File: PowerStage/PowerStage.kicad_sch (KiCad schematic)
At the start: 27 parts, among them J1 Conn_01x02, J2 Conn_01x02, J3 Conn_01x03, Q1 IRFZ44N, Q2 IRFZ44N, SW2 SW_SPDT_XKB_DMx-xxxx-1, U1 IR2110

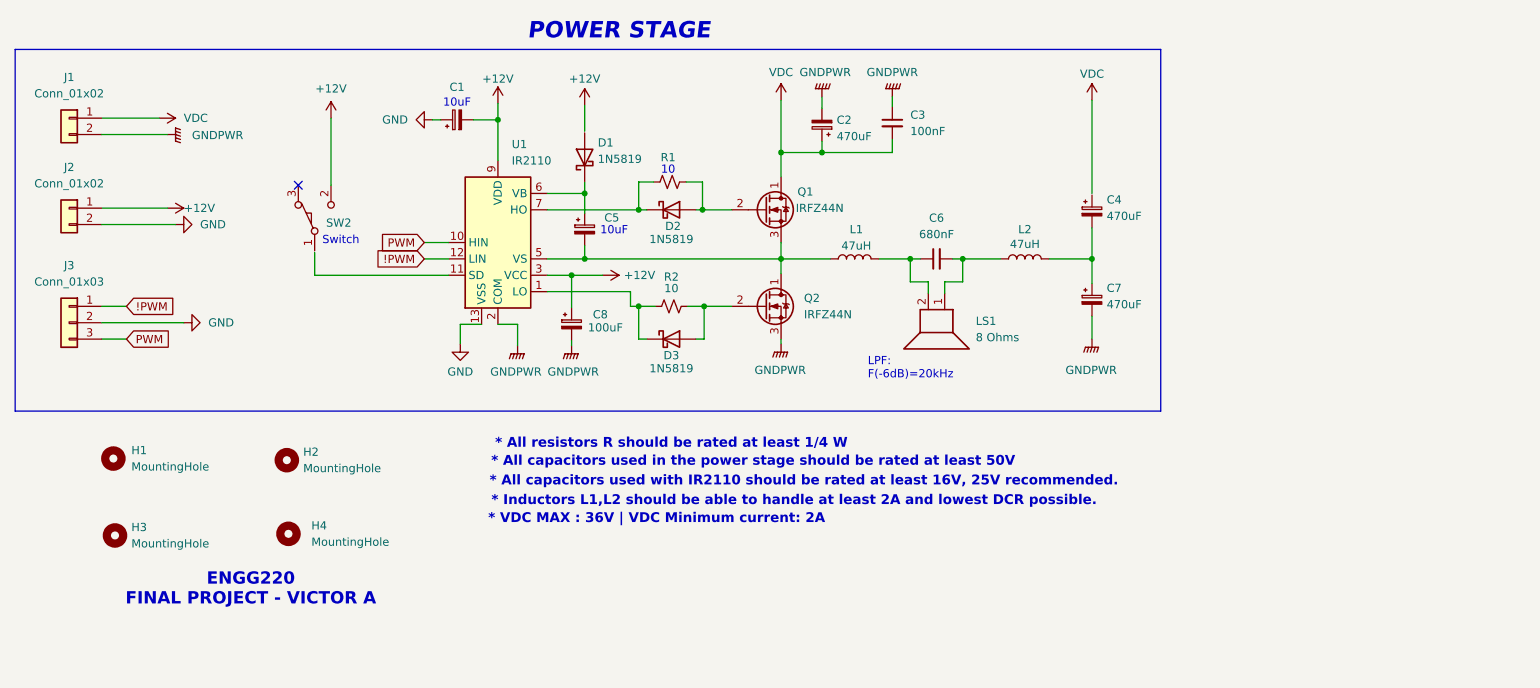
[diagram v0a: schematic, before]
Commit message: Init Full Bridge Topology
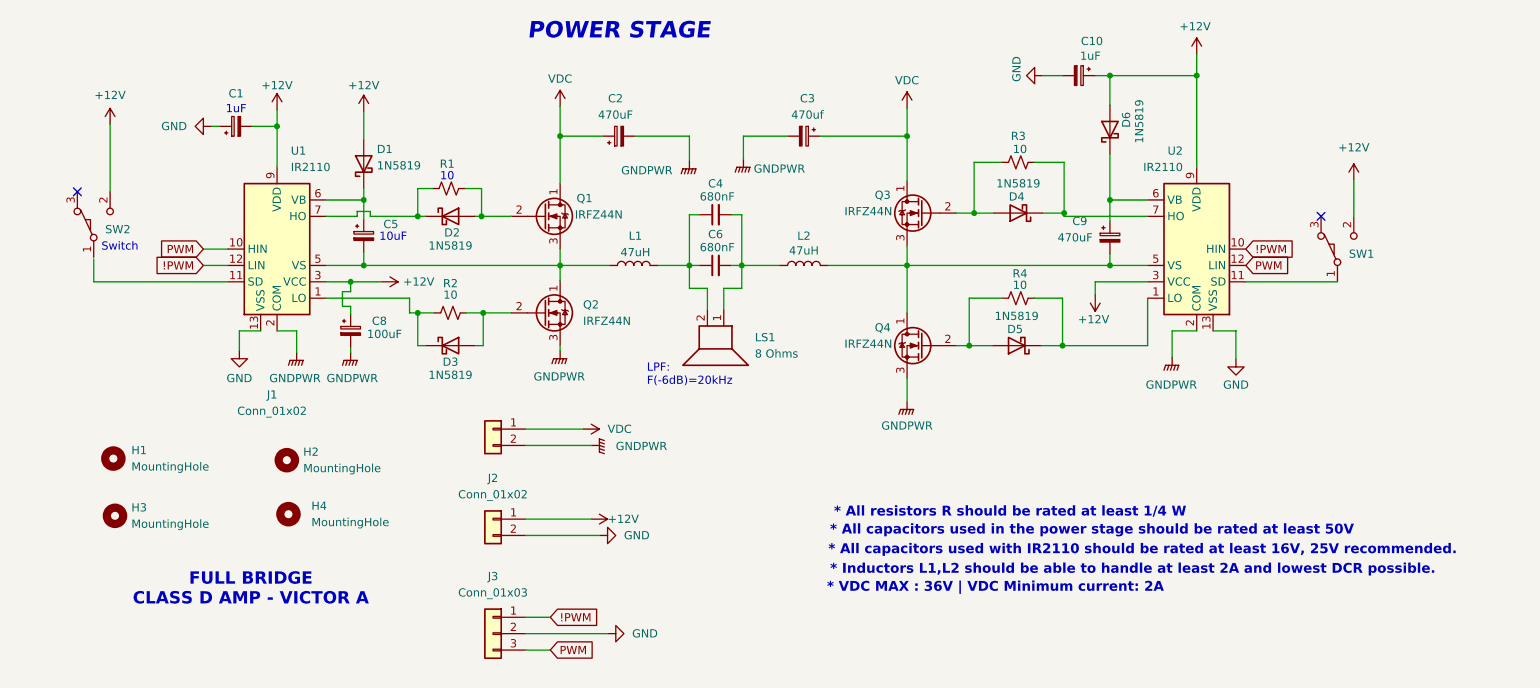
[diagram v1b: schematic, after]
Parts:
- removed C3: 100nF, symbol Device:C_Small
- removed C4, C7: 470uF, symbol Device:C_Polarized_Small
- added C10: 1uF, symbol Device:C_Polarized_Small
- added C3: 470uf, symbol Device:C_Polarized_Small
- added C4: 680nF, symbol Device:C_Small
- added C9: 470uF, symbol Device:C_Polarized_Small
- added D4, D5, D6: 1N5819, Diode_THT:D_DO-41_SOD81_P10.16mm_Horizontal, symbol Diode:1N5819
- added Q3, Q4: IRFZ44N, Package_DirectFET:DirectFET_MF, symbol Transistor_FET:IRF40DM229
- added R3, R4: 10, symbol Device:R_Small_US
- added SW1: SW_SPDT_XKB_DMx-xxxx-1, symbol Switch:SW_SPDT_XKB_DMx-xxxx-1
- added U2: IR2110, Package_DIP:DIP-14_W7.62mm, symbol Driver_FET:IR2110
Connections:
- net !PWM: now also U2.10 (HIN)
- net +12V: now also D1.2 (A), C10.1, D6.2 (A), SW1.2 (B), U2.3 (VCC), U2.9 (VDD)
- net GND: now also C10.2, U2.13 (VSS)
- net GNDPWR: now also C3.2, Q4.3 (S), U2.2 (COM)
- net PWM: now also U2.12 (LIN)
- net VDC: now also C3.1, Q3.1 (D)
- net at L2.2: now also C9.2, Q3.3 (S), Q4.1 (D), U2.5 (VS)
- net at C6.2, L2.1, LS1.1: now also C4.2
- net at C6.1, L1.2, LS1.2: now also C4.1
- net at C5.2, Q1.3 (S), Q2.1 (D)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: now also L1.1
- new net: D4.2 (A), Q3.2 (G), R3.1
- new net: C9.1, D6.1 (K), U2.6 (VB)
- new net: SW1.1 (A), U2.11 (SD)
- new net: D4.1 (K), R3.2, U2.7 (HO)
- new net: D5.2 (A), Q4.2 (G), R4.1
- new net: D5.1 (K), R4.2, U2.1 (LO)
- no-connect marks 1 -> 2
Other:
- note added: "1uF"
- note added: "FULL BRIDGE CLASS D AMP - VICTOR A"
- note removed: "ENGG220 FINAL PROJECT - VICTOR A"
- moved on the sheet: C1, C5, C6, C8, D1, D2, D3, H3, H4, J1, J2, J3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

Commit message: Init pcb layout
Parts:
- removed SW1, SW2: SW_SPDT_XKB_DMx-xxxx-1, symbol Switch:SW_SPDT_XKB_DMx-xxxx-1
- added C11, C7: 100nF, Capacitor_THT:CP_Radial_D12.5mm_P5.00mm, symbol Device:C_Polarized_Small
- added JP1, JP2: SolderJumper_2_Open, Jumper:SolderJumper-2_P1.3mm_Open_Pad1.0x1.5mm, symbol Jumper:SolderJumper_2_Open
- added R5, R6: 10k, Resistor_THT:R_Axial_DIN0207_L6.3mm_D2.5mm_P7.62mm_Horizontal, symbol Device:R_Small_US
- C1, C10, C5: footprint (none) -> Capacitor_THT:CP_Radial_D5.0mm_P2.00mm
- C2, C3: footprint (none) -> Capacitor_THT:CP_Radial_D12.5mm_P5.00mm
- C4, C6: footprint (none) -> Capacitor_THT:C_Rect_L24.0mm_W8.3mm_P22.50mm_MKT
- C8: footprint (none) -> Capacitor_THT:CP_Radial_D8.0mm_P3.80mm
- C9: value 470uF -> 10uF; footprint (none) -> Capacitor_THT:CP_Radial_D5.0mm_P2.00mm
- H1, H2, H3, H4: footprint (none) -> MountingHole:MountingHole_3.2mm_M3_Pad_Via
- J1, J2: footprint (none) -> Connector_JST:JST_XH_B2B-XH-A_1x02_P2.50mm_Vertical
- J3: footprint (none) -> Connector_JST:JST_XH_B3B-XH-A_1x03_P2.50mm_Vertical
- L1, L2: footprint (none) -> Inductor_SMD:L_12x12mm_H6mm
- LS1: footprint (none) -> Connector_JST:JST_VH_B2P-VH_1x02_P3.96mm_Vertical
- Q1, Q2, Q3, Q4: footprint Package_DirectFET:DirectFET_MF -> Package_TO_SOT_THT:TO-220-3_Vertical
- R1, R2, R3, R4: footprint (none) -> Resistor_THT:R_Axial_DIN0207_L6.3mm_D2.5mm_P7.62mm_Horizontal
- U1, U2: footprint Package_DIP:DIP-14_W7.62mm -> Package_DIP:DIP-14_W7.62mm_Socket
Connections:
- net +12V: now also JP1.2 (B), JP2.2 (B)
- net GND: now also R5.2, R6.2
- net GNDPWR: now also C11.2, C7.2
- net VDC: now also C11.1, C7.1
- net at U2.11 (SD): now also JP1.1 (A), R5.1
- net at U1.11 (SD): now also JP2.1 (A), R6.1
- no-connect marks 2 -> 0
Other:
- note removed: "Switch"
- moved on the sheet: J1, J2, J3

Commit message: PCB desing init
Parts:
- added TP1, TP2, TP3, TP4, TP5, TP6, TP7, TP8, TP9: TestPoint, TestPoint:TestPoint_Keystone_5010-5014_Multipurpose, symbol Connector:TestPoint
- C11, C7: footprint Capacitor_THT:CP_Radial_D12.5mm_P5.00mm -> Capacitor_THT:C_Disc_D3.8mm_W2.6mm_P2.50mm
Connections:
- net +12V: now also R5.2, R6.2; no longer JP1.2 (B), JP2.2 (B)
- net GND: now also JP1.2 (B), JP2.2 (B), TP9.1; no longer R5.2, R6.2
- net GNDPWR: now also TP4.1, TP8.1
- net at D4.2 (A), Q3.2 (G), R3.1: now also TP5.1
- net at C9.2, L2.2, Q3.3 (S)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: now also TP6.1
- net at C5.2, L1.1, Q1.3 (S)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: now also TP2.1
- net at D3.2 (A), Q2.2 (G), R2.2: now also TP3.1
- net at D2.2 (A), Q1.2 (G), R1.2: now also TP1.1
- net at D5.2 (A), Q4.2 (G), R4.1: now also TP7.1

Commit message: Rev 1.0 Gerber
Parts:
- J1: footprint Connector_JST:JST_XH_B2B-XH-A_1x02_P2.50mm_Vertical -> Connector_JST:JST_VH_B2P-VH_1x02_P3.96mm_Vertical
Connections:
- net at C4.1, C6.1, LS1.2: now also L1.1; no longer L1.2
- net at C5.2, Q1.3 (S), Q2.1 (D)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: now also L1.2; no longer L1.1
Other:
- moved on the sheet: L1
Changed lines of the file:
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@@
 		(on_board yes)
 		(dnp no)
-		(fields_autoplaced yes)
 		(property "Reference" "R6"
 			(at 41.91 59.1819 0)
@@
 					(size 1.27 1.27)
 				)
-				(justify left)
+				(justify right)
 			)
 		)
@@
 			)
 		)
-		(property "Footprint" "Connector_JST:JST_XH_B2B-XH-A_1x02_P2.50mm_Vertical"
+		(property "Footprint" "Connector_JST:JST_VH_B2P-VH_1x02_P3.96mm_Vertical"
 			(at 92.202 80.264 0)
 			(effects
@@
 	(symbol
 		(lib_id "Device:L")
-		(at 112.268 52.324 90)
+		(at 112.268 52.324 270)
+		(mirror x)
 		(unit 1)
 		(exclude_from_sim no)
@@
 		(dnp no)
 		(property "Reference" "L1"
-			(at 112.522 47.752 90)
+			(at 112.014 47.752 90)
 			(effects
 				(font
@@
 		)
 		(property "Value" "47uH"
-			(at 112.522 50.292 90)
+			(at 112.014 50.292 90)
 			(effects
 				(font

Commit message: Revision 1.1 in progress
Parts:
- removed C4: 680nF, Capacitor_THT:C_Rect_L24.0mm_W8.3mm_P22.50mm_MKT, symbol Device:C_Small
- removed JP1, JP2: SolderJumper_2_Open, Jumper:SolderJumper-2_P1.3mm_Open_Pad1.0x1.5mm, symbol Jumper:SolderJumper_2_Open
- removed Q1, Q2, Q3, Q4: IRFZ44N, Package_TO_SOT_THT:TO-220-3_Vertical, symbol Transistor_FET:IRF40DM229
- removed R5, R6: 10k, Resistor_THT:R_Axial_DIN0207_L6.3mm_D2.5mm_P7.62mm_Horizontal, symbol Device:R_Small_US
- added C12: 100nF 1206, Capacitor_SMD:C_1206_3216Metric, symbol Device:C_Small
- added C13: 100nF-1206, Capacitor_SMD:C_1206_3216Metric, symbol Device:C_Small
- added Q1, Q2, Q3, Q4: IRFB4227PBF, lcsc_footprints:C2652_TO-220-3_L10_0-W4_5-P2_54-L, symbol lcsc_imported:IRFB4227PBF
- added R5, R6: 10k-1206, Resistor_SMD:R_1206_3216Metric, symbol Device:R_Small
- added SW1, SW2: K2-2235D-F1, lcsc_footprints:C108742_SW-TH_K2-2235D-F1, symbol lcsc_imported:K2-2235D-F1
- R1, R2, R3, R4: footprint Resistor_THT:R_Axial_DIN0207_L6.3mm_D2.5mm_P7.62mm_Horizontal -> Resistor_SMD:R_1206_3216Metric
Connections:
- net +12V: now also C1.1, SW1.1, SW2.1; no longer C1.2
- net GND: now also C1.2, C11.2, C2.2, C3.2, C7.2, C8.2, J1.2 (Pin_2), TP8.1, U1.2 (COM), U2.2 (COM), C12.2, C13.2, Q2.3 (S), Q4.3 (S), R5.2, R6.2, SW1.3, SW2.3; no longer C1.1
- net VDC: now also Q1.2 (D), Q3.2 (D)
- net at C9.2, L2.2, TP6.1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: now also Q3.3 (S), Q4.2 (D)
- net at D4.2 (A), R3.1, TP5.1: now also Q3.1 (G)
- net at D2.2 (A), R1.2, TP1.1: now also Q1.1 (G)
- net at C5.2, L1.2, TP2.1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: now also Q1.3 (S), Q2.2 (D)
- net at D3.2 (A), R2.2, TP3.1: now also Q2.1 (G)
- net at D5.2 (A), R4.1, TP7.1: now also Q4.1 (G)
- net at U1.11 (SD): now also C12.1, R5.1, SW1.2
- net at U2.11 (SD): now also C13.1, R6.1, SW2.2
- removed net GNDPWR: C11.2, C2.2, C3.2, C7.2, C8.2, J1.2 (Pin_2), TP4.1, TP8.1, U1.2 (COM), U2.2 (COM)
- no-connect marks 0 -> 6
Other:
- moved on the sheet: C1, C10, C11, C6, C7

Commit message: Rev 1.1 progress
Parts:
- removed L1, L2: 47uH, Inductor_SMD:L_12x12mm_H6mm, symbol Device:L
- added C4: 100uF, Capacitor_THT:CP_Radial_D8.0mm_P3.80mm, symbol Device:C_Polarized_Small
- added L1, L2: MDA1365-470M, lcsc_footprints:C2847587_IND-SMD_L13_5-W12_6_TMPA1265SP-100MN-D, symbol lcsc_imported:MDA1365-470M
- C11, C7: footprint Capacitor_THT:C_Disc_D3.8mm_W2.6mm_P2.50mm -> Capacitor_SMD:C_1206_3216Metric
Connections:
- net +12V: now also C4.1
- net GND: now also C4.2
- net at D2.2 (A), R1.2, TP1.1: no longer Q1.1 (G)
- net at C5.2, Q1.3 (S), Q2.2 (D)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: now also L1.1
- net at C6.2, LS1.1: now also L2.1
- net at C6.1, LS1.2: now also L1.2
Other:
- note added: "* VDC MAX : 36V | VDC Maximum current: 2A"
- note removed: "* VDC MAX : 36V | VDC Minimum current: 2A"

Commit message: PCB layout progress
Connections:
- net at C9.2, Q3.3 (S), Q4.2 (D)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: now also L2.2
- net at L2.1, LS1.1: now also C6.1; no longer C6.2
- net at L1.2, LS1.2: now also C6.2; no longer C6.1
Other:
- moved on the sheet: C6
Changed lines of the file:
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@@
 	)
 	(junction
-		(at 154.686 52.324)
+		(at 154.94 52.07)
 		(diameter 0)
 		(color 0 0 0 0)
@@
 	(wire
 		(pts
-			(xy 154.686 52.324) (xy 154.686 59.69)
+			(xy 154.94 52.07) (xy 154.686 59.69)
 		)
 		(stroke
@@
 	(wire
 		(pts
-			(xy 154.686 52.324) (xy 162.56 52.324)
+			(xy 154.94 52.07) (xy 162.56 52.324)
 		)
 		(stroke
@@
 	(wire
 		(pts
-			(xy 154.686 49.276) (xy 154.686 52.324)
+			(xy 154.686 49.276) (xy 154.94 52.07)
 		)
 		(stroke
@@
 	(symbol
 		(lib_id "Device:C_Small")
-		(at 124.968 47.244 90)
+		(at 124.968 47.244 270)
+		(mirror x)
 		(unit 1)
 		(exclude_from_sim no)
@@
 		)
 		(property "Value" "680nF"
-			(at 125.222 44.45 90)
+			(at 124.714 44.45 90)
 			(effects
 				(font
@@
 		(on_board yes)
 		(dnp no)
-		(fields_autoplaced yes)
 		(property "Reference" "L2"
 			(at 142.24 45.72 0)

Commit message: PCB layout progress
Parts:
- removed C2: 470uF, Capacitor_THT:CP_Radial_D12.5mm_P5.00mm, symbol Device:C_Polarized_Small
- removed C3: 470uf, Capacitor_THT:CP_Radial_D12.5mm_P5.00mm, symbol Device:C_Polarized_Small
- added C2, C3: 470uF 16V, lcsc_footprints:C3341_CAP-SMD_BD8_0-L8_3-W8_3-FD, symbol lcsc_imported:470uF_16V
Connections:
- net GND: now also C2.2, C3.2
- net VDC: now also C2.1, C3.1
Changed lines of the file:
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@@
 	)
 	(junction
-		(at 165.1 44.196)
+		(at 154.686 32.258)
 		(diameter 0)
 		(color 0 0 0 0)
 	)
 	(junction
-		(at 88.646 44.704)
+		(at 165.1 44.196)
 		(diameter 0)
 		(color 0 0 0 0)
 	)
 	(junction
-		(at 100.838 32.258)
+		(at 88.646 44.704)
 		(diameter 0)
 		(color 0 0 0 0)
@@
 	)
 	(junction
-		(at 211.582 54.864)
+		(at 100.838 30.226)
 		(diameter 0)
 		(color 0 0 0 0)
 	)
 	(junction
-		(at 87.376 59.69)
+		(at 211.582 54.864)
 		(diameter 0)
 		(color 0 0 0 0)
 	)
 	(junction
-		(at 154.686 32.258)
+		(at 87.376 59.69)
 		(diameter 0)
 		(color 0 0 0 0)
@@
 	(wire
 		(pts
+			(xy 129.286 32.258) (xy 134.874 32.258)
+		)
+		(stroke
+			(width 0)
+			(type default)
+		)
+	)
+	(wire
+		(pts
 			(xy 186.182 50.546) (xy 186.182 52.324)
 		)
@@
 	(wire
 		(pts
+			(xy 154.686 32.258) (xy 154.686 34.29)
+		)
+		(stroke
+			(width 0)
+			(type default)
+		)
+	)
+	(wire
+		(pts
 			(xy 216.916 54.864) (xy 216.916 57.15)
 		)
@@
 	(wire
 		(pts
-			(xy 100.838 32.258) (xy 100.838 33.528)
-		)
-		(stroke
-			(width 0)
-			(type default)
-		)
-	)
-	(wire
-		(pts
 			(xy 165.1 44.196) (xy 165.1 36.322)
 		)
@@
 	(wire
 		(pts
-			(xy 154.686 34.29) (xy 154.686 32.258)
+			(xy 154.686 27.94) (xy 154.686 32.258)
 		)
 		(stroke
@@
 	(wire
 		(pts
-			(xy 154.686 27.94) (xy 154.686 32.258)
-		)
-		(stroke
-			(width 0)
-			(type default)
-		)
-	)
-	(wire
-		(pts
 			(xy 162.306 44.196) (xy 165.1 44.196)
 		)
@@
 	(wire
 		(pts
+			(xy 113.538 30.226) (xy 120.904 30.226)
+		)
+		(stroke
+			(width 0)
+			(type default)
+		)
+	)
+	(wire
+		(pts
 			(xy 97.282 109.474) (xy 101.092 109.474)
 		)
@@
 	(wire
 		(pts
+			(xy 100.838 30.226) (xy 100.838 33.528)
+		)
+		(stroke
+			(width 0)
+			(type default)
+		)
+	)
+	(wire
+		(pts
 			(xy 178.816 57.404) (xy 178.816 64.77)
 		)
@@
 	(wire
 		(pts
+			(xy 100.838 30.226) (xy 105.918 30.226)
+		)
+		(stroke
+			(width 0)
+			(type default)
+		)
+	)
+	(wire
+		(pts
 			(xy 207.264 54.864) (xy 211.582 54.864)
 		)
@@
 	(wire
 		(pts
-			(xy 100.838 27.686) (xy 100.838 32.258)
+			(xy 100.838 27.686) (xy 100.838 30.226)
 		)
 		(stroke
@@
 	(wire
 		(pts
-			(xy 112.522 32.258) (xy 120.904 32.258)
-		)
-		(stroke
-			(width 0)
-			(type default)
-		)
-	)
-	(wire
-		(pts
 			(xy 166.37 56.388) (xy 162.306 56.388)
 		)
@@
 	(wire
 		(pts
-			(xy 120.904 32.258) (xy 120.904 36.068)
+			(xy 120.904 30.226) (xy 120.904 36.068)
 		)
 		(stroke
@@
 	(wire
 		(pts
-			(xy 69.342 44.704) (xy 69.342 43.942)
+			(xy 142.494 32.258) (xy 154.686 32.258)
 		)
 		(stroke
@@
 	(wire
 		(pts
-			(xy 141.224 32.258) (xy 154.686 32.258)
-		)
-		(stroke
-			(width 0)
-			(type default)
-		)
-	)
-	(wire
-		(pts
-			(xy 100.838 32.258) (xy 107.442 32.258)
+			(xy 69.342 44.704) (xy 69.342 43.942)
 		)
 		(stroke
@@
 	(wire
 		(pts
-			(xy 129.286 32.258) (xy 136.144 32.258)
-		)
-		(stroke
-			(width 0)
-			(type default)
-		)
-	)
-	(wire
-		(pts
 			(xy 44.196 61.976) (xy 44.196 63.5)
 		)
@@
 	)
 	(symbol
-		(lib_id "Device:C_Polarized_Small")
-		(at 109.982 32.258 90)
+		(lib_id "lcsc_imported:470uF_16V")
+		(at 109.728 30.226 0)
 		(unit 1)
 		(exclude_from_sim no)
@@
 		(fields_autoplaced yes)
 		(property "Reference" "C2"
-			(at 109.4359 26.416 90)
+			(at 109.1209 23.368 0)
 			(effects
 				(font
@@
 			)
 		)
-		(property "Value" "470uF"
-			(at 109.4359 28.956 90)
+		(property "Value" "470uF 16V"
+			(at 109.1209 25.908 0)
 			(effects
 				(font
@@
 			)
 		)
-		(property "Footprint" "Capacitor_THT:CP_Radial_D12.5mm_P5.00mm"
-			(at 109.982 32.258 0)
+		(property "Footprint" "lcsc_footprints:C3341_CAP-SMD_BD8_0-L8_3-W8_3-FD"
+			(at 109.728 40.386 0)
 			(effects
 				(font
@@
 			)
 		)
-		(property "Datasheet" "~"
-			(at 109.982 32.258 0)
+		(property "Datasheet" "https://wmsc.lcsc.com/wmsc/upload/file/pdf/v2/lcsc/2304140030_Honor-Elec-RVT1C471M0810_C3341.pdf"
+			(at 107.442 30.099 0)
 			(effects
 				(font
@@
 			)
 		)
-		(property "Description" "Polarized capacitor, small symbol"
-			(at 109.982 32.258 0)
+		(property "Description" "470uF 16V"
+			(at 109.728 30.226 0)
+			(effects
+				(font
+					(size 1.27 1.27)
+				)
+				(hide yes)
+			)
+		)
+		(property "LCSC" "C3341"
+			(at 109.728 30.226 0)
+			(effects
+				(font
+					(size 1.27 1.27)
+				)
+				(hide yes)
+			)
+		)
+		(property "Manufacturer" "HONOR(荣誉)"
+			(at 109.728 30.226 0)
 			(effects
 				(font
@@
 	)
 	(symbol
-		(lib_id "Device:C_Polarized_Small")
-		(at 138.684 32.258 270)
-		(unit 1)
-		(exclude_from_sim no)
-		(in_bom yes)
-		(on_board yes)
-		(dnp no)
-		(fields_autoplaced yes)
-		(property "Reference" "C3"
-			(at 139.2301 26.416 90)
-			(effects
-				(font
-					(size 1.27 1.27)
-				)
-			)
-		)
-		(property "Value" "470uf"
-			(at 139.2301 28.956 90)
-			(effects
-				(font
-					(size 1.27 1.27)
-				)
-			)
-		)
-		(property "Footprint" "Capacitor_THT:CP_Radial_D12.5mm_P5.00mm"
-			(at 138.684 32.258 0)
-			(effects
-				(font
-					(size 1.27 1.27)
-				)
-				(hide yes)
-			)
-		)
-		(property "Datasheet" "~"
-			(at 138.684 32.258 0)
-			(effects
-				(font
-					(size 1.27 1.27)
-				)
-				(hide yes)
-			)
-		)
-		(property "Description" "Polarized capacitor, small symbol"
-			(at 138.684 32.258 0)
-			(effects
-				(font
-					(size 1.27 1.27)
-				)
-				(hide yes)
-			)
-		)
-		(pin "2"
-		)
-		(pin "1"
-		)
-		(instances
-			(project "PowerStage"
-				(path "/35e7ada8-13ff-43aa-b843-352fc42c8474"
-					(reference "C3")
-					(unit 1)
-				)
-			)
-		)
-	)
-	(symbol
 		(lib_id "Device:C_Small")
 		(at 44.196 59.436 0)
@@
 					(unit 1)
 				)
+			)
+		)
+	)
+	(symbol
+		(lib_id "lcsc_imported:470uF_16V")
+		(at 138.684 32.258 180)
+		(unit 1)
+		(exclude_from_sim no)
+		(in_bom yes)
+		(on_board yes)
+		(dnp no)
+		(fields_autoplaced yes)
+		(property "Reference" "C3"
+			(at 139.291 25.654 0)
+			(effects
+				(font
+					(size 1.27 1.27)
+				)
+			)
+		)
+		(property "Value" "470uF 16V"
+			(at 139.291 28.194 0)
+			(effects
+				(font
+					(size 1.27 1.27)
+				)
+			)
+		)
+		(property "Footprint" "lcsc_footprints:C3341_CAP-SMD_BD8_0-L8_3-W8_3-FD"
+			(at 138.684 22.098 0)
+			(effects
+				(font
+					(size 1.27 1.27)
+				)
+				(hide yes)
+			)
+		)
+		(property "Datasheet" "https://wmsc.lcsc.com/wmsc/upload/file/pdf/v2/lcsc/2304140030_Honor-Elec-RVT1C471M0810_C3341.pdf"
+			(at 140.97 32.385 0)
+			(effects
+				(font
+					(size 1.27 1.27)
+				)
+				(hide yes)
+			)
+		)
+		(property "Description" "470uF 16V"
+			(at 138.684 32.258 0)
+			(effects
+				(font
+					(size 1.27 1.27)
+				)
+				(hide yes)
+			)
+		)
+		(property "LCSC" "C3341"
+			(at 138.684 32.258 0)
+			(effects
+				(font
+					(size 1.27 1.27)
+				)
+				(hide yes)
+			)
+		)
+		(property "Manufacturer" "HONOR(荣誉)"
+			(at 138.684 32.258 0)
+			(effects
+				(font
+					(size 1.27 1.27)
+				)
+				(hide yes)
+			)
+		)
+		(pin "2"
+		)
+		(pin "1"
+		)
+		(instances
+			(project "PowerStage"
+				(path "/35e7ada8-13ff-43aa-b843-352fc42c8474"
+					(reference "C3")
+					(unit 1)
+				)
